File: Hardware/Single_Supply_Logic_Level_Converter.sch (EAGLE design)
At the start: 23 parts, among them U1 TXB0104, U2 TPS61200, U4 MIC5219-3.3

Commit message: Updating design per review
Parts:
- removed H1, H2: STAND-OFFTIGHT, SparkFun-Hardware:STAND-OFFTIGHT
- removed LED1: RED, SparkFun-LED:LED-RED0603
- removed R7: 1K, SparkFun:RESISTOR0402-RES
- removed U4: MIC5219-3.3, SparkFun:V_REG_LDOSMD
- added C7: 10uF, SparkFun-Capacitors:10UF-POLAR-EIA3216-16V-10%(TANT)
- added D1: RED, SparkFun-LED:LED-RED0603
- added FD1, FD2, FD3, FD4: FIDUCIALUFIDUCIAL, SparkFun-Aesthetics:FIDUCIALUFIDUCIAL
- added J3, J4: (no value), SparkFun-Connectors:CONN_01
- added JP1: JUMPER-SMT_3_1-NC_TRACE_SILK, SparkFun-Jumpers:JUMPER-SMT_3_1-NC_TRACE_SILK
- added JP2: JUMPER-SMT_2_NC_TRACE_SILK, SparkFun-Jumpers:JUMPER-SMT_2_NC_TRACE_SILK
- added LOGO3: SFE_LOGO_FLAME.1_INCH, SparkFun-Aesthetics:SFE_LOGO_FLAME.1_INCH
- added LOGO4: OSHW-LOGOS, SparkFun-Aesthetics:OSHW-LOGOS
- added R3: 1k, SparkFun-Resistors:1KOHM-0603-1/10W-1%
- added R4: 13k, SparkFun-Resistors:13KOHM-0603-1/10W-1%
- added R5: 22k, SparkFun-Resistors:22KOHM-0603-1/10W-1%
- added R6: (no value), SparkFun-Resistors:RESISTORAXIAL-0.3
- added U3: ADJ, SparkFun-IC-Power:V_REG_MIC5205ADJ
- C4: value 10uF -> 470pF; device SparkFun:CAP_POL1206 -> SparkFun-Capacitors:470PF-0603-50V-5%
- C5: device SparkFun:CAP0603-CAP -> SparkFun-Capacitors:0.1UF-0603-25V-5%
- C6: device CH_passive:CAP1206 -> SparkFun-Capacitors:10UF-0603-6.3V-20%
- JP3: device SparkFun-Connectors:CONN_03 -> SparkFun-Connectors:CONN_04
- U2: device SparkFun:TPS61200 -> SparkFun-IC-Power:TPS61200
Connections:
- removed net 3.3V: C1.1, C4.+, JP3.3, R7.2, U1.OE, U1.VCCA, U4.OUT
- removed net N$4: LED1.A, R7.1
- new net N$1: JP1.3, U3.OUT
- new net N$11: C4.1, R4.1, R5.2, R6.1, U3.BP
- new net N$12: JP2.1, R4.2
- new net N$3: D1.A, R3.1
- new net VCCA: C1.1, C7.+, JP1.1, JP1.2, JP2.2, JP3.3, R3.2, R6.2, U1.OE, U1.VCCA
- net 5V: now also U3.EN, U3.IN; no longer U4.EN, U4.IN
- net GND: now also C4.2, C7.-, D1.C, J3.1, J4.1, JP3.4, R5.1, U3.GND; no longer C4.-, LED1.C, U4.GND
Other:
- note added: "Default VCCA = 3.3V"
- note added: "Solder right side of JP1 and cut trace between JP2 to use PTH resistor to set VCCA."
- note added: "WARNING: If setting output to 1.8V do not exceed 80mA."
- moved on the sheet: C1, C2, C3, C5, C6, J1, J2, JP7, L1, R1, R2, U1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

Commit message: New labels
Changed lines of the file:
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@@
 <part name="LOGO3" library="SparkFun-Aesthetics" deviceset="SFE_LOGO_FLAME" device=".1_INCH" value="SFE_LOGO_FLAME.1_INCH"/>
 <part name="LOGO4" library="SparkFun-Aesthetics" deviceset="OSHW-LOGO" device="S"/>
+<part name="GND-ISO1" library="SparkFun-PowerSymbols" deviceset="GND-ISO" device=""/>
 </parts>
 <sheets>
@@
 <instance part="LOGO3" gate="G$1" x="134.62" y="45.72"/>
 <instance part="LOGO4" gate="G$1" x="236.22" y="48.26"/>
+<instance part="GND-ISO1" gate="G$1" x="30.48" y="88.9"/>
 </instances>
 <busses>

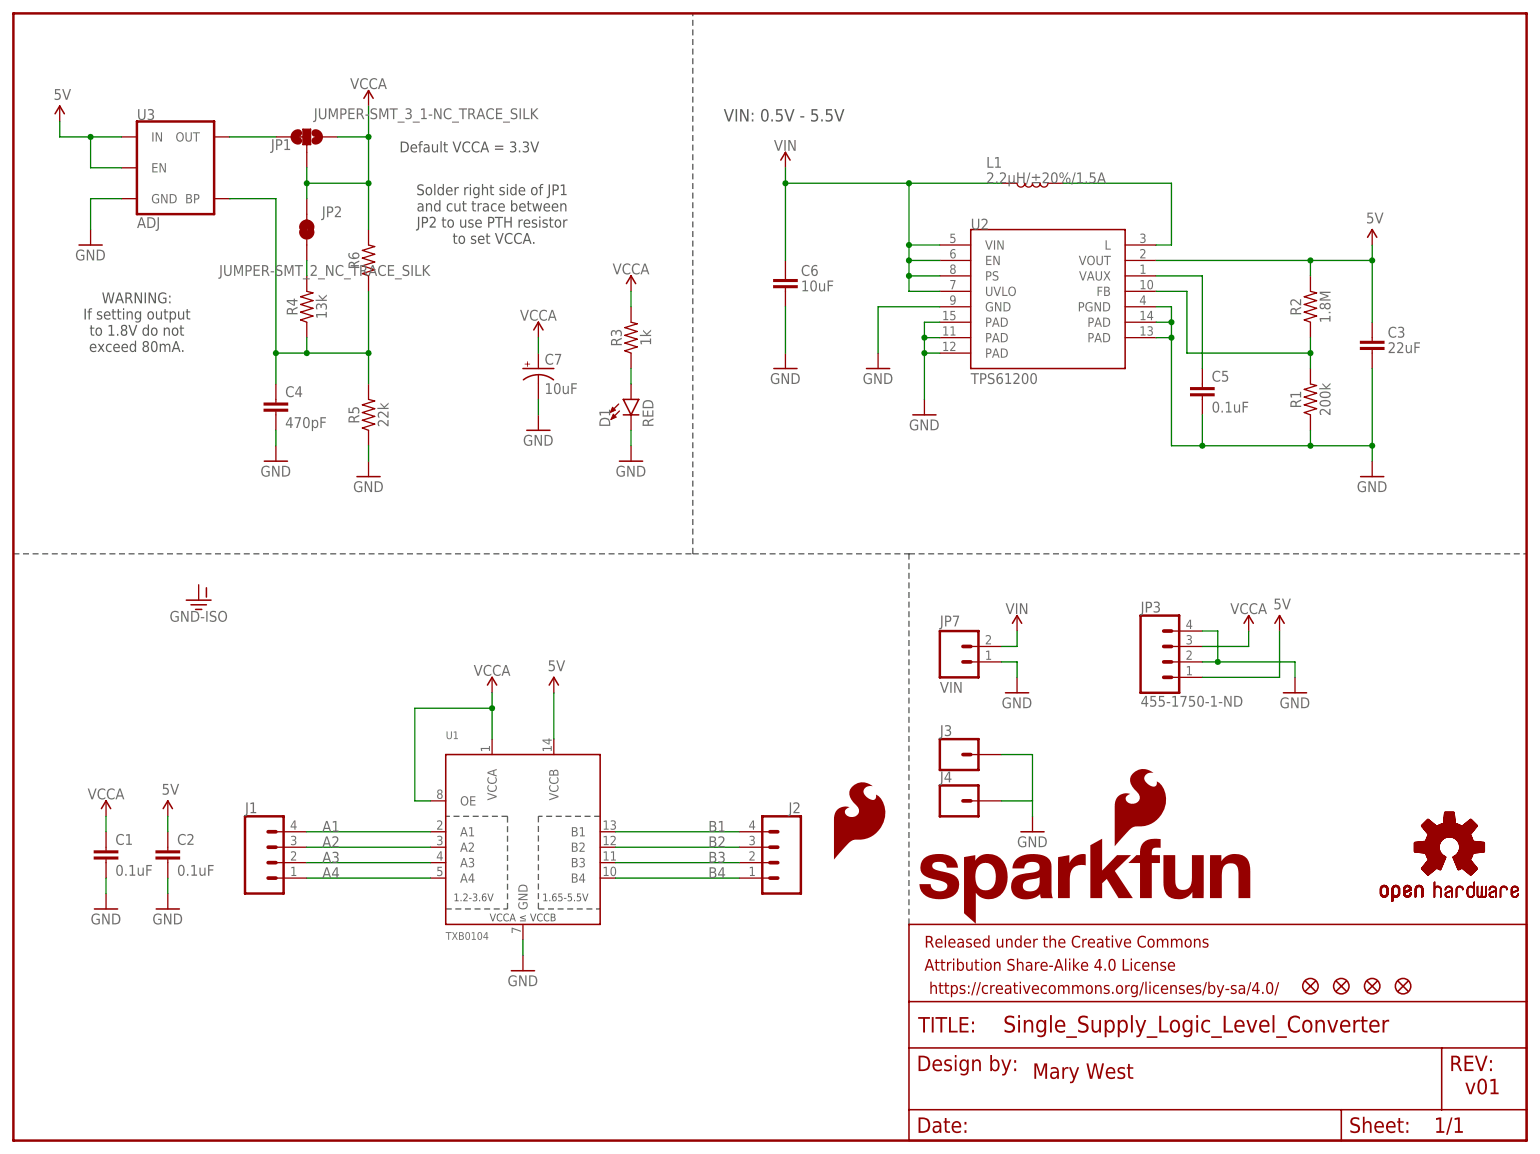
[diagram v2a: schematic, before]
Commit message: Added text for warnings and jumper settings
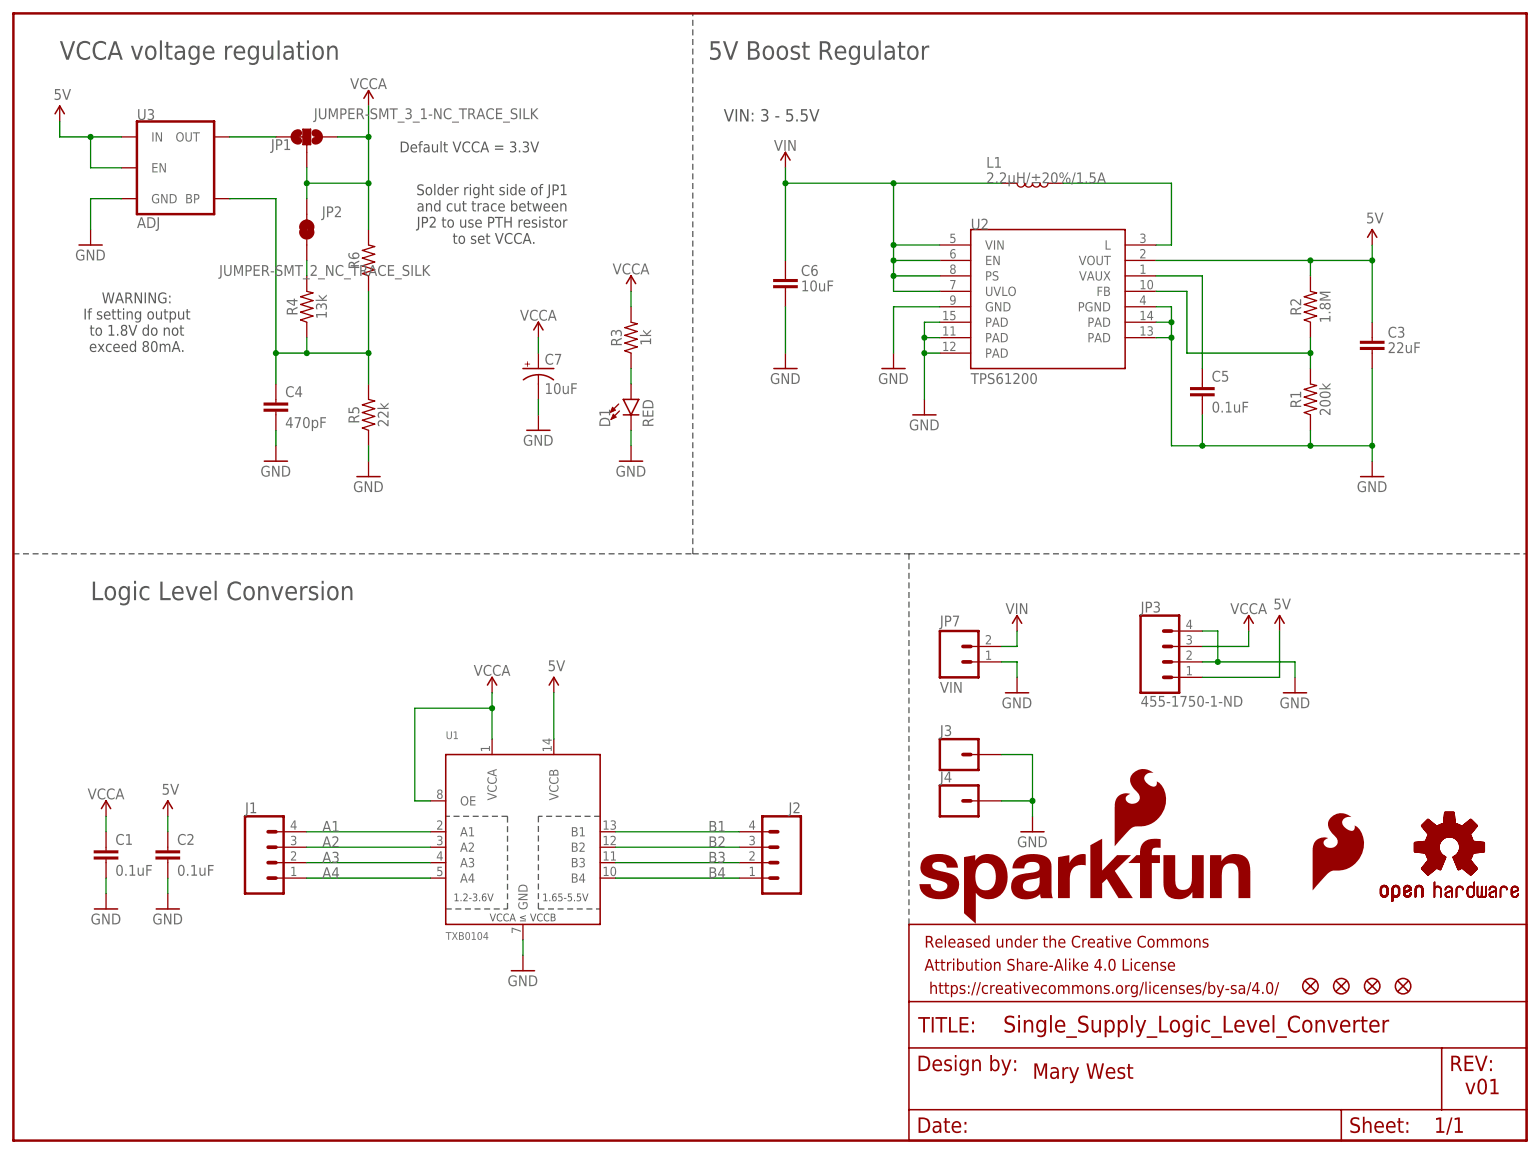
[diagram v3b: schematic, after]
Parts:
- C3: device CH_passive:CAP0805 -> SparkFun-Capacitors:22UF-0805-6.3V-20%
- C5: device SparkFun-Capacitors:0.1UF-0603-25V-5% -> SparkFun-Capacitors:0.1UF-0603-25V-(+80/-20%)
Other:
- note added: "5V Boost Regulator"
- note added: "Logic Level Conversion"
- note added: "VCCA voltage regulation"
- note added: "VIN: 3 - 5.5V"
- note removed: "VIN: 0.5V - 5.5V"

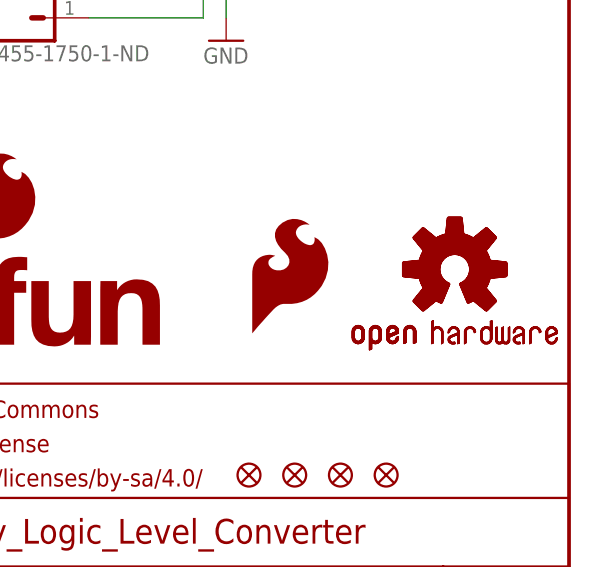
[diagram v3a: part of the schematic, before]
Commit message: adding buzzard labels
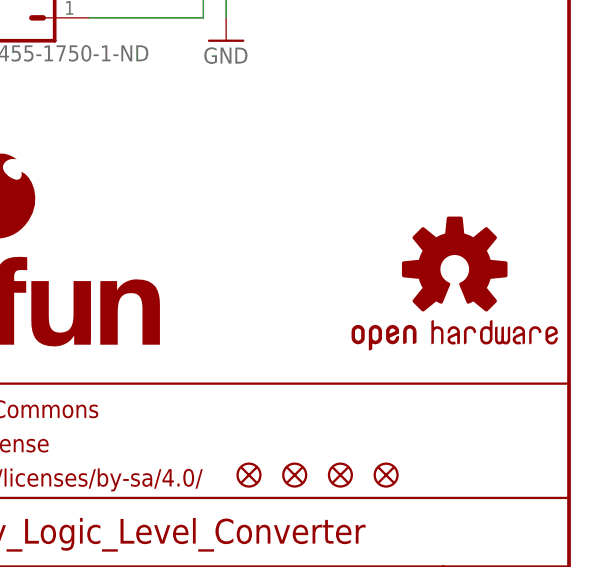
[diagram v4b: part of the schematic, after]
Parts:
- removed LOGO3: SFE_LOGO_FLAME.1_INCH, SparkFun-Aesthetics:SFE_LOGO_FLAME.1_INCH
- removed LOGO4: OSHW-LOGOS, SparkFun-Aesthetics:OSHW-LOGOS
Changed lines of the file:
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@@
 <grid distance="0.1" unitdist="inch" unit="inch" style="lines" multiple="1" display="no" altdistance="0.01" altunitdist="inch" altunit="inch"/>
 <layers>
-<layer number="1" name="Top" color="4" fill="1" visible="yes" active="no"/>
-<layer number="2" name="Route2" color="1" fill="3" visible="yes" active="no"/>
-<layer number="3" name="Route3" color="4" fill="3" visible="yes" active="no"/>
-<layer number="4" name="Route4" color="1" fill="4" visible="yes" active="no"/>
-<layer number="5" name="Route5" color="4" fill="4" visible="yes" active="no"/>
-<layer number="6" name="Route6" color="1" fill="8" visible="yes" active="no"/>
-<layer number="7" name="Route7" color="4" fill="8" visible="yes" active="no"/>
-<layer number="8" name="Route8" color="1" fill="2" visible="yes" active="no"/>
-<layer number="9" name="Route9" color="4" fill="2" visible="yes" active="no"/>
-<layer number="10" name="Route10" color="1" fill="7" visible="yes" active="no"/>
-<layer number="11" name="Route11" color="4" fill="7" visible="yes" active="no"/>
-<layer number="12" name="Route12" color="1" fill="5" visible="yes" active="no"/>
-<layer number="13" name="Route13" color="4" fill="5" visible="yes" active="no"/>
-<layer number="14" name="Route14" color="1" fill="6" visible="yes" active="no"/>
-<layer number="15" name="Route15" color="4" fill="6" visible="yes" active="no"/>
-<layer number="16" name="Bottom" color="1" fill="1" visible="yes" active="no"/>
-<layer number="17" name="Pads" color="2" fill="1" visible="yes" active="no"/>
-<layer number="18" name="Vias" color="2" fill="1" visible="yes" active="no"/>
-<layer number="19" name="Unrouted" color="6" fill="1" visible="yes" active="no"/>
-<layer number="20" name="Dimension" color="6" fill="1" visible="yes" active="no"/>
-<layer number="21" name="tPlace" color="6" fill="1" visible="yes" active="no"/>
-<layer number="22" name="bPlace" color="6" fill="1" visible="yes" active="no"/>
-<layer number="23" name="tOrigins" color="15" fill="1" visible="yes" active="no"/>
-<layer number="24" name="bOrigins" color="15" fill="1" visible="yes" active="no"/>
-<layer number="25" name="tNames" color="7" fill="1" visible="yes" active="no"/>
-<layer number="26" name="bNames" color="7" fill="1" visible="yes" active="no"/>
-<layer number="27" name="tValues" color="7" fill="1" visible="yes" active="no"/>
-<layer number="28" name="bValues" color="7" fill="1" visible="yes" active="no"/>
+<layer number="1" name="Top" color="4" fill="1" visible="no" active="no"/>
+<layer number="2" name="Route2" color="1" fill="3" visible="no" active="no"/>
+<layer number="3" name="Route3" color="4" fill="3" visible="no" active="no"/>
+<layer number="4" name="Route4" color="1" fill="4" visible="no" active="no"/>
+<layer number="5" name="Route5" color="4" fill="4" visible="no" active="no"/>
+<layer number="6" name="Route6" color="1" fill="8" visible="no" active="no"/>
+<layer number="7" name="Route7" color="4" fill="8" visible="no" active="no"/>
+<layer number="8" name="Route8" color="1" fill="2" visible="no" active="no"/>
+<layer number="9" name="Route9" color="4" fill="2" visible="no" active="no"/>
+<layer number="10" name="Route10" color="1" fill="7" visible="no" active="no"/>
+<layer number="11" name="Route11" color="4" fill="7" visible="no" active="no"/>
+<layer number="12" name="Route12" color="1" fill="5" visible="no" active="no"/>
+<layer number="13" name="Route13" color="4" fill="5" visible="no" active="no"/>
+<layer number="14" name="Route14" color="1" fill="6" visible="no" active="no"/>
+<layer number="15" name="Route15" color="4" fill="6" visible="no" active="no"/>
+<layer number="16" name="Bottom" color="1" fill="1" visible="no" active="no"/>
+<layer number="17" name="Pads" color="2" fill="1" visible="no" active="no"/>
+<layer number="18" name="Vias" color="2" fill="1" visible="no" active="no"/>
+<layer number="19" name="Unrouted" color="6" fill="1" visible="no" active="no"/>
+<layer number="20" name="Dimension" color="6" fill="1" visible="no" active="no"/>
+<layer number="21" name="tPlace" color="6" fill="1" visible="no" active="no"/>
+<layer number="22" name="bPlace" color="6" fill="1" visible="no" active="no"/>
+<layer number="23" name="tOrigins" color="15" fill="1" visible="no" active="no"/>
+<layer number="24" name="bOrigins" color="15" fill="1" visible="no" active="no"/>
+<layer number="25" name="tNames" color="7" fill="1" visible="no" active="no"/>
+<layer number="26" name="bNames" color="7" fill="1" visible="no" active="no"/>
+<layer number="27" name="tValues" color="7" fill="1" visible="no" active="no"/>
+<layer number="28" name="bValues" color="7" fill="1" visible="no" active="no"/>
 <layer number="29" name="tStop" color="7" fill="3" visible="no" active="no"/>
 <layer number="30" name="bStop" color="7" fill="6" visible="no" active="no"/>
@@
 <layer number="35" name="tGlue" color="7" fill="4" visible="no" active="no"/>
 <layer number="36" name="bGlue" color="7" fill="5" visible="no" active="no"/>
-<layer number="37" name="tTest" color="7" fill="1" visible="yes" active="no"/>
-<layer number="38" name="bTest" color="7" fill="1" visible="yes" active="no"/>
+<layer number="37" name="tTest" color="7" fill="1" visible="no" active="no"/>
+<layer number="38" name="bTest" color="7" fill="1" visible="no" active="no"/>
 <layer number="39" name="tKeepout" color="4" fill="11" visible="no" active="no"/>
 <layer number="40" name="bKeepout" color="1" fill="11" visible="no" active="no"/>
@@
 <layer number="44" name="Drills" color="7" fill="1" visible="no" active="no"/>
 <layer number="45" name="Holes" color="7" fill="1" visible="no" active="no"/>
-<layer number="46" name="Milling" color="3" fill="1" visible="yes" active="no"/>
-<layer number="47" name="Measures" color="7" fill="1" visible="yes" active="no"/>
-<layer number="48" name="Document" color="7" fill="1" visible="yes" active="no"/>
-<layer number="49" name="Reference" color="7" fill="1" visible="yes" active="no"/>
-<layer number="50" name="dxf" color="7" fill="1" visible="yes" active="no"/>
-<layer number="51" name="tDocu" color="6" fill="1" visible="yes" active="no"/>
-<layer number="52" name="bDocu" color="7" fill="1" visible="yes" active="no"/>
-<layer number="53" name="tGND_GNDA" color="7" fill="9" visible="yes" active="no"/>
-<layer number="54" name="bGND_GNDA" color="1" fill="9" visible="yes" active="no"/>
-<layer number="56" name="wert" color="7" fill="1" visible="yes" active="no"/>
-<layer number="57" name="tCAD" color="7" fill="1" visible="yes" active="no"/>
-<layer number="59" name="tCarbon" color="7" fill="1" visible="yes" active="no"/>
-<layer number="60" name="bCarbon" color="7" fill="1" visible="yes" active="no"/>
+<layer number="46" name="Milling" color="3" fill="1" visible="no" active="no"/>
+<layer number="47" name="Measures" color="7" fill="1" visible="no" active="no"/>
+<layer number="48" name="Document" color="7" fill="1" visible="no" active="no"/>
+<layer number="49" name="Reference" color="7" fill="1" visible="no" active="no"/>
+<layer number="50" name="dxf" color="7" fill="1" visible="no" active="no"/>
+<layer number="51" name="tDocu" color="6" fill="1" visible="no" active="no"/>
+<layer number="52" name="bDocu" color="7" fill="1" visible="no" active="no"/>
+<layer number="53" name="tGND_GNDA" color="7" fill="9" visible="no" active="no"/>
+<layer number="54" name="bGND_GNDA" color="1" fill="9" visible="no" active="no"/>
+<layer number="56" name="wert" color="7" fill="1" visible="no" active="no"/>
+<layer number="57" name="tCAD" color="7" fill="1" visible="no" active="no"/>
+<layer number="59" name="tCarbon" color="7" fill="1" visible="no" active="no"/>
+<layer number="60" name="bCarbon" color="7" fill="1" visible="no" active="no"/>
 <layer number="88" name="SimResults" color="9" fill="1" visible="no" active="yes"/>
 <layer number="89" name="SimProbes" color="9" fill="1" visible="no" active="yes"/>
@@
 <layer number="255" name="routoute" color="7" fill="1" visible="yes" active="yes"/>
 </layers>
-<schematic xreflabel="%F%N/%S.%C%R" xrefpart="/%S.%C%R">
+<schematic xreflabel="%F%N/%S" xrefpart="/%S.%C%R">
 <attributes>
 </attributes>
@@
 <part name="J4" library="SparkFun-Connectors" deviceset="CONN_01" device=""/>
 <part name="GND15" library="SparkFun" deviceset="GND" device=""/>
-<part name="LOGO3" library="SparkFun-Aesthetics" deviceset="SFE_LOGO_FLAME" device=".1_INCH" value="SFE_LOGO_FLAME.1_INCH"/>
-<part name="LOGO4" library="SparkFun-Aesthetics" deviceset="OSHW-LOGO" device="S"/>
 </parts>
 <sheets>
@@
 <instance part="J4" gate="G$1" x="154.94" y="55.88"/>
 <instance part="GND15" gate="1" x="167.64" y="50.8"/>
-<instance part="LOGO3" gate="G$1" x="213.36" y="40.64"/>
-<instance part="LOGO4" gate="G$1" x="236.22" y="48.26"/>
 </instances>
 <busses>
